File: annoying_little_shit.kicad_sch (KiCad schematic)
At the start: 15 parts, among them J1 Conn_01x06_Pin, Q1 Si2319CDS, Q2 MMBT3904, U1 ATtiny13V-10SU

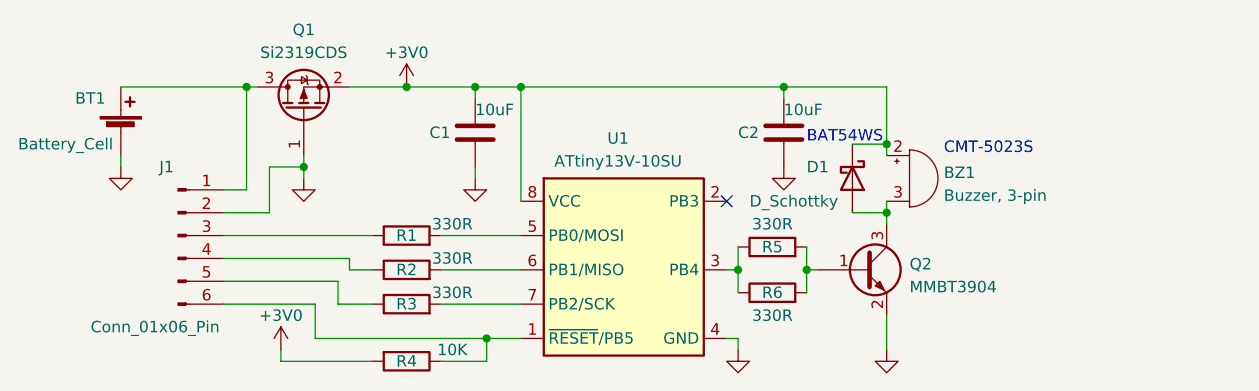
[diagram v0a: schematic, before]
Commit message: Version 1.0: Current limiting resistor on buzzer, larger footprint for buzzer to make it easier to solder, remove pull-up on nRST to limit current drain (there should also be an internal one on the AVR
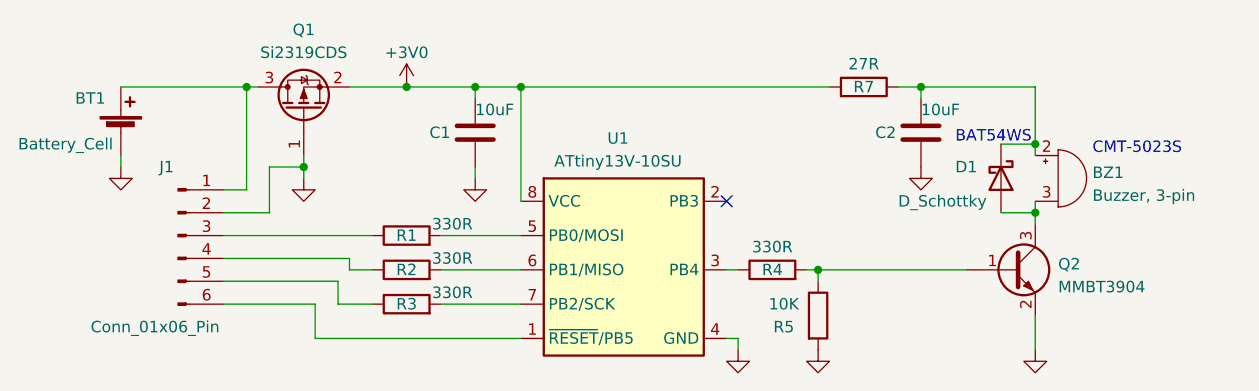
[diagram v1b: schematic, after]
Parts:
- removed R4: 10K, Resistor_SMD:R_0603_1608Metric, symbol Device:R
- removed R6: 330R, Resistor_SMD:R_0603_1608Metric, symbol Device:R
- added R5: 10K, Resistor_SMD:R_0603_1608Metric, symbol Device:R
- added R7: 27R, Resistor_SMD:R_0603_1608Metric, symbol Device:R
- J1: footprint Connector_PinHeader_1.27mm:PinHeader_1x06_P1.27mm_Vertical_SMD_Pin1Left -> als_footprints:PinHeader_1x06_P1.00mm_Vertical_SMD_Aligned
- renumbered R5 to R4
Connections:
- net +3V0: now also R7.2; no longer BZ1.2 (+), C2.1, D1.1 (K)
- net GND: now also R5.2
- net at Q2.1 (B), R4.2: now also R5.1
- new net: BZ1.2 (+), C2.1, D1.1 (K), R7.1
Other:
- moved on the sheet: BZ1, C2, D1, Q2, R4
